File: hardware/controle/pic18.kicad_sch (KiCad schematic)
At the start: 10 parts, among them J10 Conn_01x05_Pin, J11 PWM, J12 ADC, U5 PIC18F05Q40

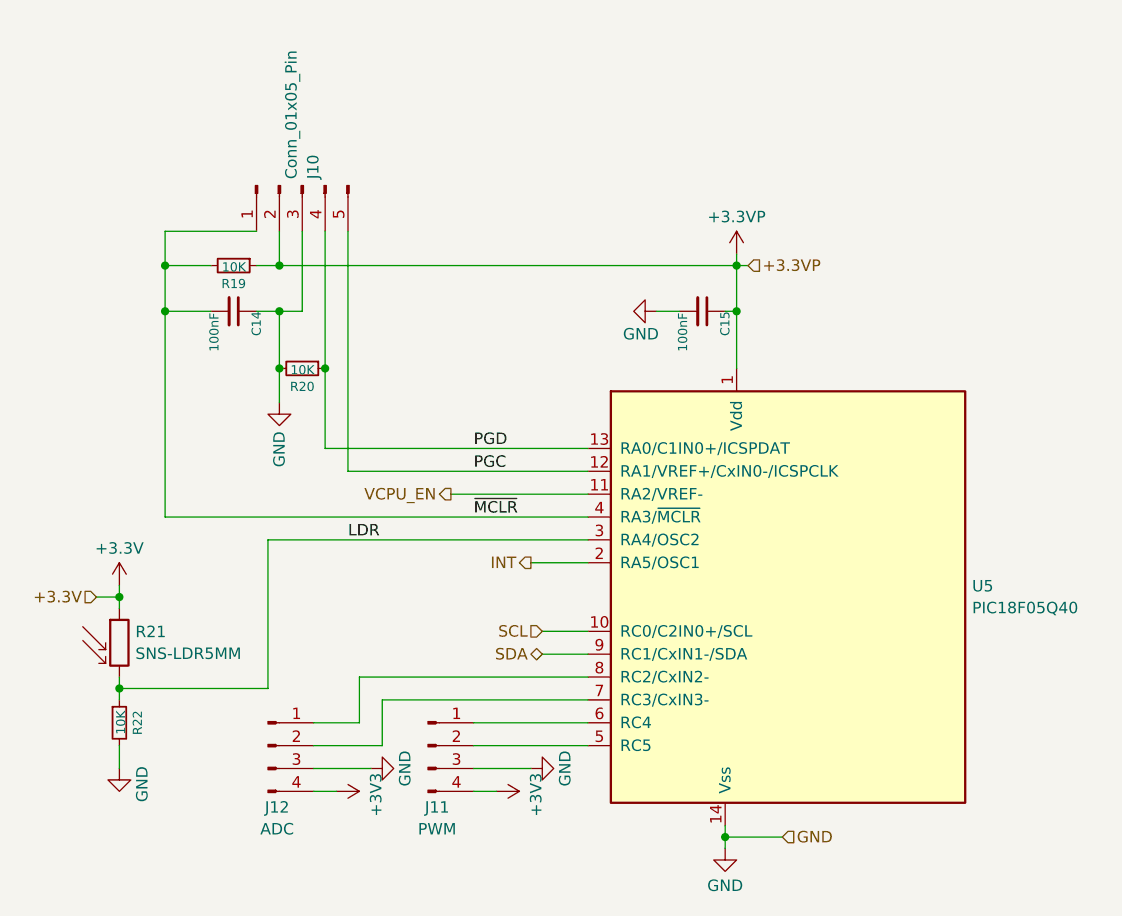
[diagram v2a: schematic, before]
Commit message: hardware/controle: route control CPU power from pic18
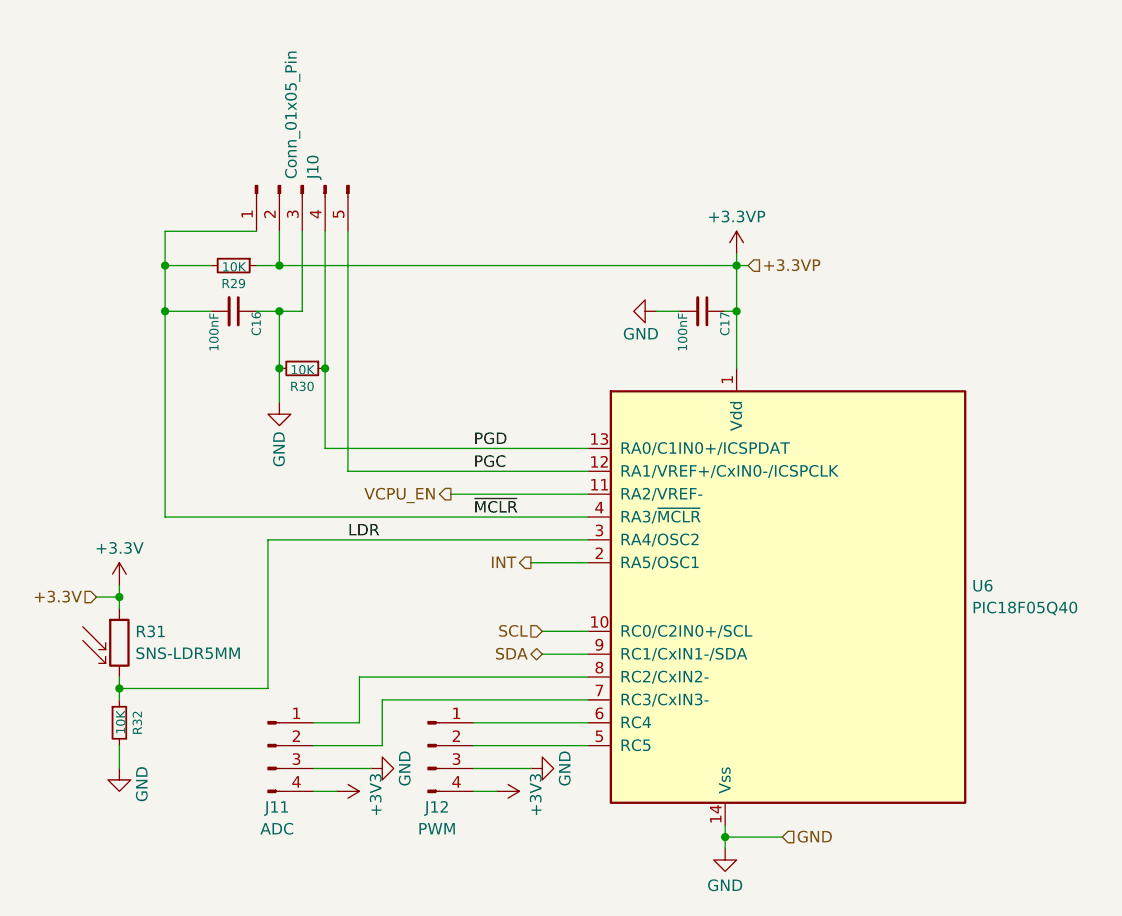
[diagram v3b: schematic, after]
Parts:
- renumbered C14 to C16, C15 to C17, J12 to J11, J11 to J12, R19 to R29, R20 to R30, R21 to R31, R22 to R32, U5 to U6
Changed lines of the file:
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@@
 		(on_board yes)
 		(dnp no)
-		(property "Reference" "#PWR028"
+		(property "Reference" "#PWR030"
 			(at 88.9 146.05 0)
 			(effects
@@
 			(project "controle"
 				(path "/41099c3f-2f7d-470d-b75f-9309d43eb2d2/3f263420-12ce-4311-9cdb-ce0ba2a241a7"
-					(reference "#PWR028")
+					(reference "#PWR030")
 					(unit 1)
 				)
@@
 		(dnp no)
 		(fields_autoplaced yes)
-		(property "Reference" "#PWR023"
+		(property "Reference" "#PWR028"
 			(at 106.68 105.41 0)
 			(effects
@@
 			(project "controle"
 				(path "/41099c3f-2f7d-470d-b75f-9309d43eb2d2/3f263420-12ce-4311-9cdb-ce0ba2a241a7"
-					(reference "#PWR023")
+					(reference "#PWR028")
 					(unit 1)
 				)
@@
 		(on_board yes)
 		(dnp no)
-		(property "Reference" "C14"
+		(property "Reference" "C16"
 			(at 104.14 88.9 0)
 			(effects
@@
 			(project "controle"
 				(path "/41099c3f-2f7d-470d-b75f-9309d43eb2d2/3f263420-12ce-4311-9cdb-ce0ba2a241a7"
-					(reference "C14")
+					(reference "C16")
 					(unit 1)
 				)
@@
 		(on_board yes)
 		(dnp no)
-		(property "Reference" "#PWR029"
+		(property "Reference" "#PWR034"
 			(at 127 142.24 0)
 			(effects
@@
 			(project "controle"
 				(path "/41099c3f-2f7d-470d-b75f-9309d43eb2d2/3f263420-12ce-4311-9cdb-ce0ba2a241a7"
-					(reference "#PWR029")
+					(reference "#PWR034")
 					(unit 1)
 				)
@@
 		(on_board yes)
 		(dnp no)
-		(property "Reference" "U5"
+		(property "Reference" "U6"
 			(at 183.642 119.4378 0)
 			(effects
@@
 			(project "controle"
 				(path "/41099c3f-2f7d-470d-b75f-9309d43eb2d2/3f263420-12ce-4311-9cdb-ce0ba2a241a7"
-					(reference "U5")
+					(reference "U6")
 					(unit 1)
 				)
@@
 		(on_board yes)
 		(dnp no)
-		(property "Reference" "R20"
+		(property "Reference" "R30"
 			(at 109.22 97.282 90)
 			(effects
@@
 			(project "controle"
 				(path "/41099c3f-2f7d-470d-b75f-9309d43eb2d2/3f263420-12ce-4311-9cdb-ce0ba2a241a7"
-					(reference "R20")
+					(reference "R30")
 					(unit 1)
 				)
@@
 		(dnp no)
 		(fields_autoplaced yes)
-		(property "Reference" "R21"
+		(property "Reference" "R31"
 			(at 90.678 124.5178 0)
 			(effects
@@
 			(project "controle"
 				(path "/41099c3f-2f7d-470d-b75f-9309d43eb2d2/3f263420-12ce-4311-9cdb-ce0ba2a241a7"
-					(reference "R21")
+					(reference "R31")
 					(unit 1)
 				)
@@
 		(on_board yes)
 		(dnp no)
-		(property "Reference" "#PWR025"
+		(property "Reference" "#PWR027"
 			(at 142.24 88.9 0)
 			(effects
@@
 			(project "controle"
 				(path "/41099c3f-2f7d-470d-b75f-9309d43eb2d2/3f263420-12ce-4311-9cdb-ce0ba2a241a7"
-					(reference "#PWR025")
+					(reference "#PWR027")
 					(unit 1)
 				)
@@
 		(on_board yes)
 		(dnp no)
-		(property "Reference" "#PWR032"
+		(property "Reference" "#PWR033"
 			(at 109.22 142.24 0)
 			(effects
@@
 			(project "controle"
 				(path "/41099c3f-2f7d-470d-b75f-9309d43eb2d2/3f263420-12ce-4311-9cdb-ce0ba2a241a7"
-					(reference "#PWR032")
+					(reference "#PWR033")
 					(unit 1)
 				)
@@
 		(on_board yes)
 		(dnp no)
-		(property "Reference" "J12"
+		(property "Reference" "J11"
 			(at 106.426 144.018 0)
 			(effects
@@
 			(project "controle"
 				(path "/41099c3f-2f7d-470d-b75f-9309d43eb2d2/3f263420-12ce-4311-9cdb-ce0ba2a241a7"
-					(reference "J12")
+					(reference "J11")
 					(unit 1)
 				)
@@
 		(on_board yes)
 		(dnp no)
-		(property "Reference" "R19"
+		(property "Reference" "R29"
 			(at 101.6 85.852 90)
 			(effects
@@
 			(project "controle"
 				(path "/41099c3f-2f7d-470d-b75f-9309d43eb2d2/3f263420-12ce-4311-9cdb-ce0ba2a241a7"
-					(reference "R19")
+					(reference "R29")
 					(unit 1)
 				)
@@
 		(dnp no)
 		(fields_autoplaced yes)
-		(property "Reference" "#PWR027"
+		(property "Reference" "#PWR035"
 			(at 156.21 154.94 0)
 			(effects
@@
 			(project "controle"
 				(path "/41099c3f-2f7d-470d-b75f-9309d43eb2d2/3f263420-12ce-4311-9cdb-ce0ba2a241a7"
-					(reference "#PWR027")
+					(reference "#PWR035")
 					(unit 1)
 				)
@@
 		(on_board yes)
 		(dnp no)
-		(property "Reference" "R22"
+		(property "Reference" "R32"
 			(at 90.932 134.62 90)
 			(effects
@@
 			(project "controle"
 				(path "/41099c3f-2f7d-470d-b75f-9309d43eb2d2/3f263420-12ce-4311-9cdb-ce0ba2a241a7"
-					(reference "R22")
+					(reference "R32")
 					(unit 1)
 				)
@@
 		(dnp no)
 		(fields_autoplaced yes)
-		(property "Reference" "#PWR024"
+		(property "Reference" "#PWR026"
 			(at 157.48 86.36 0)
 			(effects
@@
 			(project "controle"
 				(path "/41099c3f-2f7d-470d-b75f-9309d43eb2d2/3f263420-12ce-4311-9cdb-ce0ba2a241a7"
-					(reference "#PWR024")
+					(reference "#PWR026")
 					(unit 1)
 				)
@@
 		(on_board yes)
 		(dnp no)
-		(property "Reference" "J11"
+		(property "Reference" "J12"
 			(at 124.206 144.018 0)
 			(effects
@@
 			(project "controle"
 				(path "/41099c3f-2f7d-470d-b75f-9309d43eb2d2/3f263420-12ce-4311-9cdb-ce0ba2a241a7"
-					(reference "J11")
+					(reference "J12")
 					(unit 1)
 				)
@@
 		(on_board yes)
 		(dnp no)
-		(property "Reference" "#PWR030"
+		(property "Reference" "#PWR032"
 			(at 140.97 139.7 0)
 			(effects
@@
 			(project "controle"
 				(path "/41099c3f-2f7d-470d-b75f-9309d43eb2d2/3f263420-12ce-4311-9cdb-ce0ba2a241a7"
-					(reference "#PWR030")
+					(reference "#PWR032")
 					(unit 1)
 				)
@@
 		(dnp no)
 		(fields_autoplaced yes)
-		(property "Reference" "#PWR026"
+		(property "Reference" "#PWR029"
 			(at 88.9 123.19 0)
 			(effects
@@
 			(project "controle"
 				(path "/41099c3f-2f7d-470d-b75f-9309d43eb2d2/3f263420-12ce-4311-9cdb-ce0ba2a241a7"
-					(reference "#PWR026")
+					(reference "#PWR029")
 					(unit 1)
 				)
@@
 		(on_board yes)
 		(dnp no)
-		(property "Reference" "C15"
+		(property "Reference" "C17"
 			(at 156.21 88.9 0)
 			(effects
@@
 			(project "controle"
 				(path "/41099c3f-2f7d-470d-b75f-9309d43eb2d2/3f263420-12ce-4311-9cdb-ce0ba2a241a7"
-					(reference "C15")
-					(unit 1)
-				)
+					(reference "C17")
+					(unit 1)
+				)

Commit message: hardware/controle: update some component values and P/N
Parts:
- C16, C17: P/N stock -> CC0805KKX7RYBB104
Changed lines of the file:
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@@
 			)
 		)
-		(property "P/N" "stock"
+		(property "P/N" "CC0805KKX7RYBB104"
 			(at 101.6 88.9 0)
 			(effects
@@
 			)
 		)
-		(property "P/N" "stock"
+		(property "P/N" "CC0805KKX7RYBB104"
 			(at 153.67 88.9 0)
 			(effects

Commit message: hardware/controle: update P/N fields
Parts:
- J10: P/N 87437-0543 -> (none)
- R29, R30, R32: P/N stock -> MCWR08X1002FTL
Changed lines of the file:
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@@
 			)
 		)
-		(property "P/N" "87437-0543"
+		(property "P/N" ""
 			(at 109.22 74.93 0)
 			(effects
@@
 			)
 		)
-		(property "P/N" "stock"
+		(property "P/N" "MCWR08X1002FTL"
 			(at 109.22 95.25 0)
 			(effects
@@
 			)
 		)
-		(property "P/N" "stock"
+		(property "P/N" "MCWR08X1002FTL"
 			(at 101.6 83.82 0)
 			(effects
@@
 			)
 		)
-		(property "P/N" "stock"
+		(property "P/N" "MCWR08X1002FTL"
 			(at 88.9 134.62 0)
 			(effects

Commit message: hardware/controle: update P/N of 100nF capacitors
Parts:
- C16, C17: P/N CC0805KKX7RYBB104 -> C0603C104K5RAC7411
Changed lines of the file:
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@@
 			)
 		)
-		(property "P/N" "CC0805KKX7RYBB104"
+		(property "P/N" "C0603C104K5RAC7411"
 			(at 101.6 88.9 0)
 			(effects
@@
 			)
 		)
-		(property "P/N" "CC0805KKX7RYBB104"
+		(property "P/N" "C0603C104K5RAC7411"
 			(at 153.67 88.9 0)
 			(effects
